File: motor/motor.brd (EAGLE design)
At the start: 78.7 x 59.4 mm, 92 parts, among them IC1 FT231XQ, P1 MF-NSML600-2, Q3 BSS138, Q4 BSS138, T1 TRANSISTORMMBT2222, T2 TRANSISTORMMBT2222, T3 TRANSISTORMMBT2222

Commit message: Update motor.
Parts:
- added C22: 47uF, FaBo-Capacitor:0603-NARROW
- added C23: 1uF, FaBo-Capacitor:0603-NARROW
- added D1: (no value), FaBo-Diode:SMBJ5.0
- added M1: (no value), FaBo-Mosfet:SOT-23
- added R32: 47K, FaBo-Resistors:0603-NARROW
- added R33: 10K, FaBo-Resistors:0603-NARROW
- added U$19: (no value), FaBo-etc:LOGO_SILK_GND
- added U$6: DUAL-PNP-TRANSISTORDMMT5401, FaBo-Transistor:SOT-26
- F1: value (none) -> 2A
- R24, R25: device FaBo-Resistors:0402 -> FaBo-Resistors:0603
- moved R1 11.1 mm to (28.9, 20.6)
- moved R2 11.0 mm to (26.5, 20.5)
- moved F1 5.26 mm to (17.9, 7.10)
- moved C6 4.97 mm to (23.0, 7.19)
- moved R24 3.93 mm to (54.3, 4.60)
- moved IC1 3.35 mm to (17.3, 17.6)
- moved C5 2.50 mm to (11.5, 19.1)
- moved R13 1.68 mm to (3.57, 7.05)
- moved R14 1.50 mm to (6.81, 6.95)
- moved R15 1.49 mm to (10.2, 6.95)
- moved T1 1.20 mm to (3.44, 10.5)
- moved T3 1.02 mm to (10.3, 10.5)
- moved T2 0.94 mm to (6.85, 10.5)
- moved R25 0.61 mm to (50.5, 4.50)
- renumbered MIC(IO5,19,22) to MIC(IO5,19,15)
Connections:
- removed net IO22: MAX1.1, U$1.P$33, U$1.P$36
- removed net N$29: U$1.P$32
- new net IO18: U$1.P$30
- new net IO23: U$1.P$32, U$1.P$37
- new net N$16: C23.2, F1.2, M1.3, U$6.6
- new net N$17: M1.1, R32.2, U$6.4
- new net N$26: R33.2, U$6.1, U$6.2, U$6.3
- net 5V: now also C22.2, D1.ANODE, M1.2, U$6.5; no longer F1.2
- net GND: now also C22.1, C23.1, D1.CATHODE, R24.1, R25.1, R32.1, R33.1; no longer R24.P$1, R25.P$1
- net IO27: now also MAX1.1
- net N$19: now also R24.2; no longer R24.P$2
- net N$25: now also R25.2; no longer R25.P$2
- net SCL: now also U$1.P$36; no longer U$1.P$37
- net SDA: now also U$1.P$33; no longer U$1.P$30
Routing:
- net IO26: track 26.0 -> 61.2 mm, vias 2 -> 0
- net IO27: track 0.00 -> 32.9 mm, vias 0 -> 2
- net USBDP: track 7.94 -> 33.8 mm, vias 0 -> 4
- net N$16: track 0.00 -> 22.3 mm
- net IO2: track 59.2 -> 37.8 mm, vias 0 -> 5
- net SCL: track 117.9 -> 102.2 mm
- net SDA: track 99.8 -> 115.3 mm, vias 2 -> 4
- net GND: track 536.6 -> 550.5 mm, vias 16 -> 28
- net N$17: track 0.00 -> 13.4 mm
- net IO22: track 12.3 -> 0.00 mm
- net N$4: track 15.3 -> 27.5 mm
- net IO34: track 39.2 -> 49.5 mm, vias 3 -> 2
- net N$3: track 31.9 -> 41.6 mm
- net IO23: track 0.00 -> 8.11 mm
- net N$7: track 15.0 -> 22.9 mm, vias 2 -> 3
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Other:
- board text added: "REV.BETA1"
- board text removed: "REV.BETA"

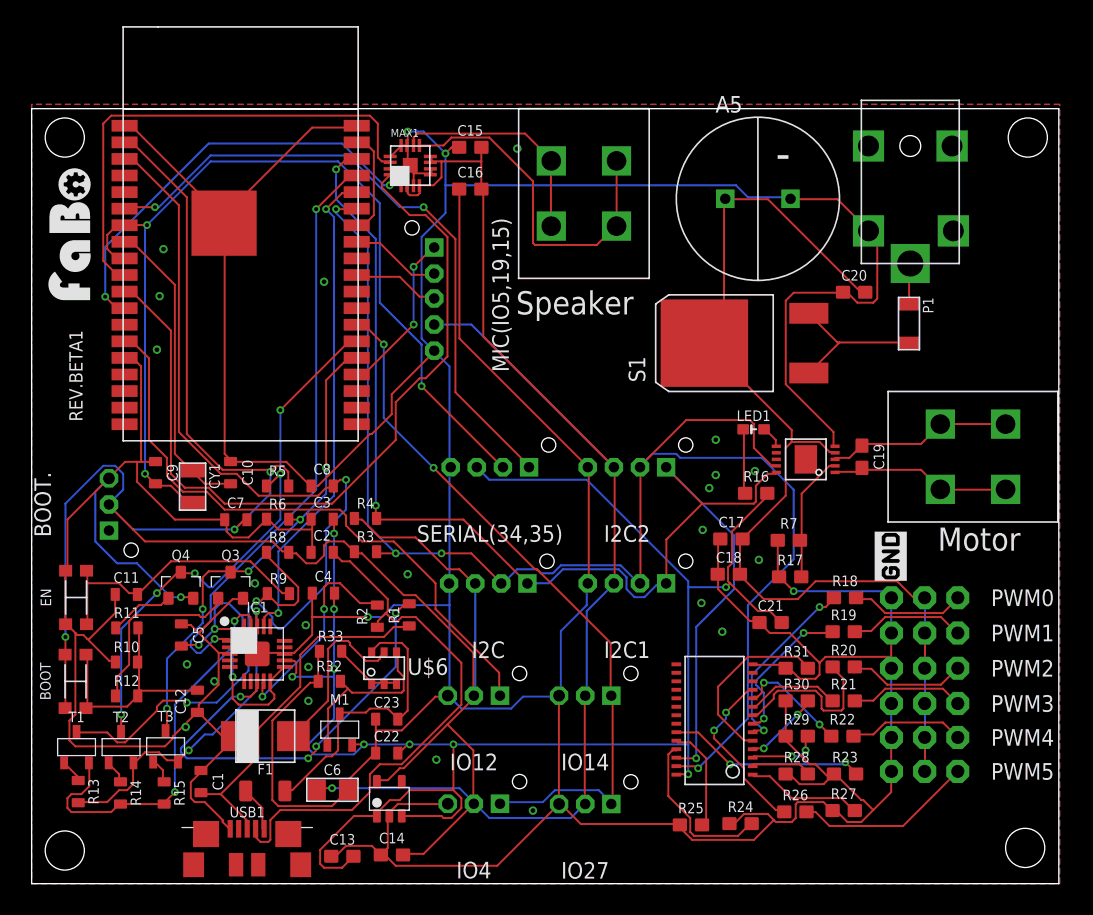
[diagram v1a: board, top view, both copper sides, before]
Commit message: Update motor.
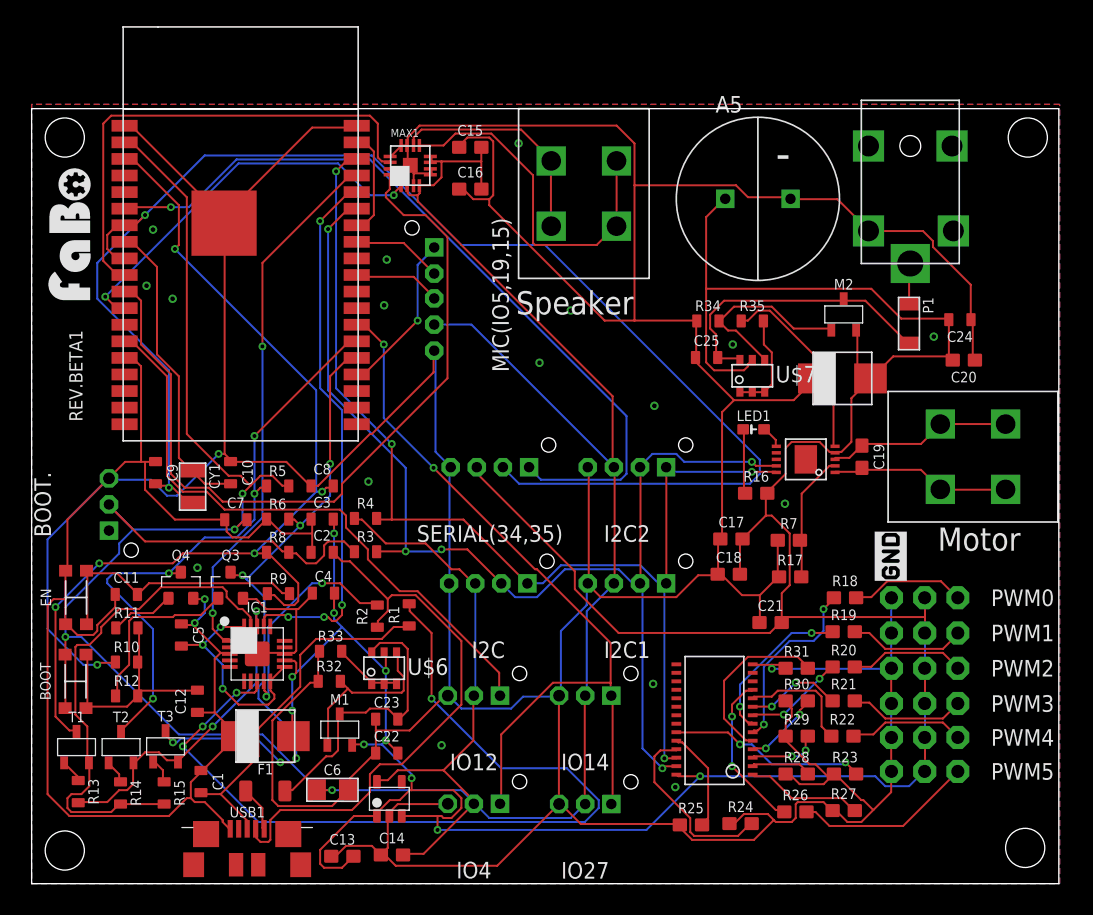
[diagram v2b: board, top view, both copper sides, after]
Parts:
- removed S1: STPS15L30CB, FaBo-Supply:STPS15L30C
- added C24: 47uF, FaBo-Capacitor:0603-NARROW
- added C25: 1uF, FaBo-Capacitor:0603-NARROW
- added D2: (no value), FaBo-Diode:SMBJ5.0
- added M2: (no value), FaBo-Mosfet:SOT-23
- added R34: 47K, FaBo-Resistors:0603-NARROW
- added R35: 10K, FaBo-Resistors:0603-NARROW
- added U$7: DUAL-PNP-TRANSISTORDMMT5401, FaBo-Transistor:SOT-26
- moved C20 9.88 mm to (71.4, 40.1), turned to 180 degrees
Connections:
- removed net VCC: A5.+, C17.2, C18.2, C20.2, PWM0.VCC, PWM1.VCC, PWM2.VCC, PWM3.VCC, PWM4.VCC, PWM5.VCC, S1.K, U$8.4
- new net N$29: M2.1, R34.2, U$7.4
- new net N$30: R35.2, U$7.1, U$7.2, U$7.3
- net 5V: now also A5.+, C17.2, C18.2, C20.2, C24.2, D2.ANODE, M2.2, PWM0.VCC, PWM1.VCC, PWM2.VCC, PWM3.VCC, PWM4.VCC, PWM5.VCC, U$7.5, U$8.4
- net GND: now also C24.1, C25.1, D2.CATHODE, R34.1, R35.1
- net N$28: now also C25.2, M2.3, U$7.6; no longer S1.A1, S1.A2
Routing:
- net 5V: track 149.3 -> 246.2 mm, vias 9 -> 10
- net VCC: track 80.7 -> 0.00 mm
- net GND: track 550.5 -> 592.3 mm, vias 28 -> 22
- net IO35: track 75.1 -> 114.7 mm, vias 3 -> 2
- net USBDP: track 33.8 -> 67.4 mm
- net SDA: track 115.3 -> 89.3 mm, vias 4 -> 5
- net N$29: track 0.00 -> 14.6 mm
- net SCL: track 102.2 -> 87.7 mm, vias 3 -> 4
- net IO2: track 37.8 -> 50.6 mm, vias 5 -> 6
- net IO34: track 49.5 -> 60.7 mm, vias 2 -> 1
- net N$28: track 11.9 -> 22.5 mm
- net EN: track 85.3 -> 76.4 mm, vias 3 -> 5
- net RTS: track 30.8 -> 39.3 mm, vias 2 -> 0
- net N$30: track 0.00 -> 7.90 mm
- net IO4: track 54.8 -> 60.7 mm
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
